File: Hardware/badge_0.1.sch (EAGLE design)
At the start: 59 parts, among them CON1 PH_2, IC1 CP2102, SW2 MK12C02, U1 SMBT2222A, U2 SMBT2222A, U4 MCP73832T-2DCI/OT

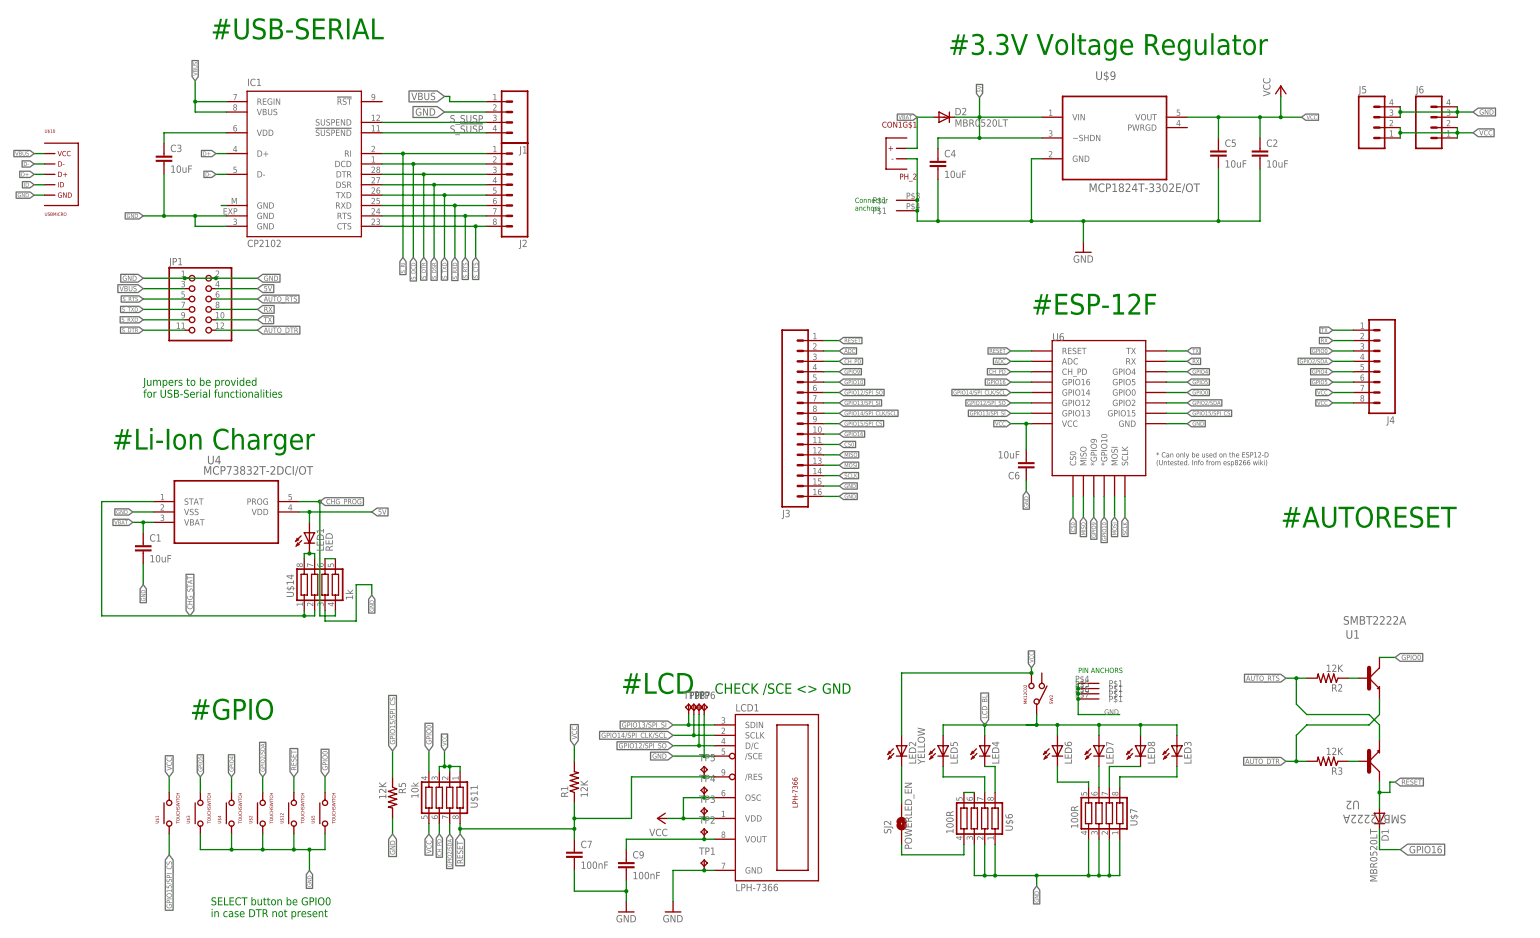
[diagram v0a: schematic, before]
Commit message: Replaced serial jumpers with a header. Thus removing the need to populate the jumpers during board assembly.
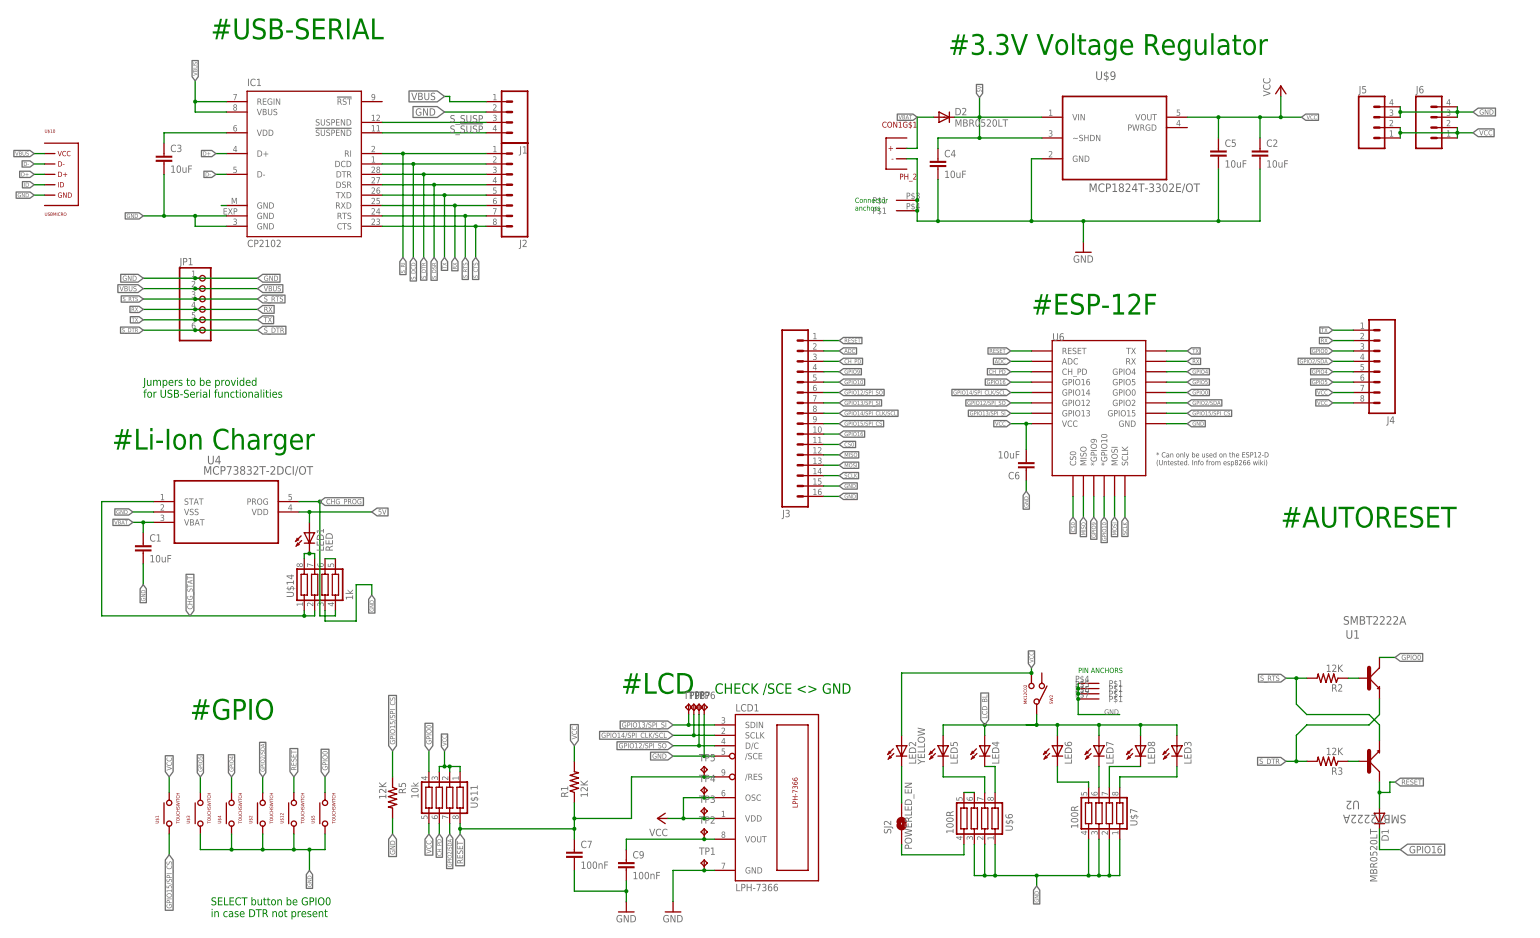
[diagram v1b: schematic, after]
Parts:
- JP1: device pinhead:PINHD-2X6 -> pinhead:PINHD-1X6
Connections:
- removed net AUTO_DTR: JP1.12, R3.2, U1.E
- removed net AUTO_RTS: JP1.6, R2.2, U2.E
- removed net S_RXD: IC1.RXD, J2.6, JP1.9
- removed net S_TXD: IC1.TXD, J2.5, JP1.7
- net 5V: no longer JP1.4
- net GND: no longer JP1.2
- net RX: now also IC1.RXD, J2.6, JP1.4; no longer JP1.8
- net S_DTR: now also JP1.6, R3.2, U1.E; no longer JP1.11
- net S_RTS: now also JP1.3, R2.2, U2.E; no longer JP1.5
- net TX: now also IC1.TXD, J2.5, JP1.5; no longer JP1.10
- net VBUS: now also JP1.2; no longer JP1.3

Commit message: Removed 12K resistor after connecting LCD & ESP resets.
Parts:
- removed R1: 12K, SparkFun-Passives:RESISTOR0805-RES
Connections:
- net RESET: no longer R1.1
- net VCC: no longer R1.2
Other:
- note added: "10K array"
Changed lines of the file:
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@@
 <part name="C6" library="SparkFun-Capacitors" deviceset="1UF-25V-10%(0805)" device="&quot;" value="10uF"/>
 <part name="C7" library="SparkFun-Capacitors" deviceset="1UF-25V-10%(0805)" device="&quot;" value="100nF"/>
-<part name="R1" library="SparkFun-Passives" deviceset="RESISTOR" device="0805-RES" value="12K"/>
 <part name="U1" library="badge" deviceset="SMBT2222A" device=""/>
 <part name="U2" library="badge" deviceset="SMBT2222A" device=""/>
@@
 anchors</text>
 <text x="271.78" y="88.9" size="1.27" layer="91" font="vector">PIN ANCHORS</text>
+<text x="148.59" y="62.23" size="1.778" layer="91" align="center">10K
+array</text>
 </plain>
 <instances>
@@
 <instance part="C6" gate="G$1" x="259.08" y="140.97" rot="R180"/>
 <instance part="C7" gate="G$1" x="148.59" y="43.18"/>
-<instance part="R1" gate="G$1" x="148.59" y="62.23" rot="R90"/>
 <instance part="U1" gate="A" x="342.9" y="87.63"/>
 <instance part="U2" gate="A" x="342.9" y="67.31" rot="MR180"/>
@@
 </segment>
 <segment>
-<pinref part="R1" gate="G$1" pin="2"/>
 <wire x1="148.59" y1="71.12" x2="148.59" y2="67.31" width="0.1524" layer="91"/>
 <label x="148.59" y="71.12" size="1.27" layer="95" rot="R90" xref="yes"/>
@@
 <pinref part="U$11" gate="G$1" pin="8"/>
 <wire x1="120.65" y1="52.07" x2="120.65" y2="50.8" width="0.1524" layer="91"/>
-<pinref part="R1" gate="G$1" pin="1"/>
 <pinref part="C7" gate="G$1" pin="1"/>
 <wire x1="120.65" y1="50.8" x2="120.65" y2="49.53" width="0.1524" layer="91"/>

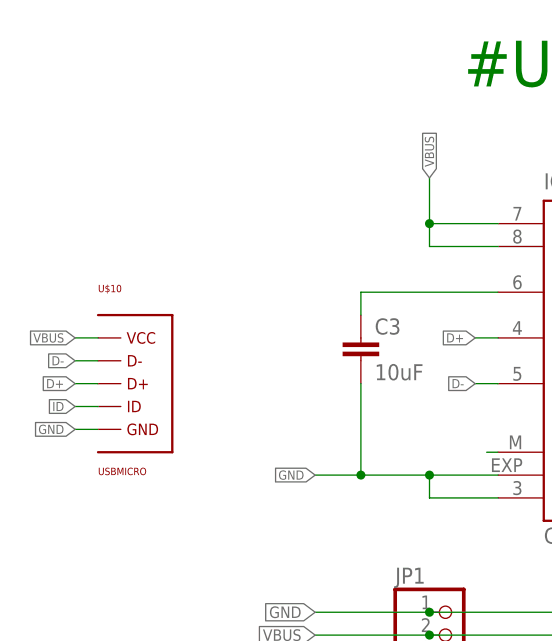
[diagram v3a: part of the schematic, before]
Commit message: moved pads and vias out of the way
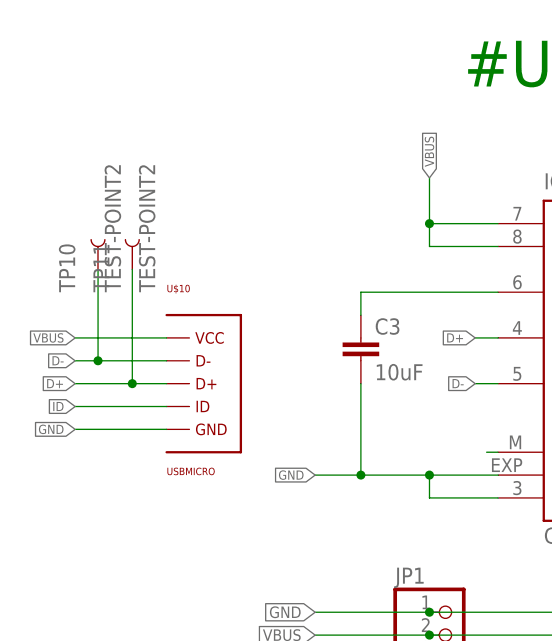
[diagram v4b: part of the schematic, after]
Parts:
- added TP10, TP11: TEST-POINT2, SparkFun-Passives:TEST-POINT2
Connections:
- net D+: now also TP11.1
- net D-: now also TP10.1
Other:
- moved on the sheet: U$10
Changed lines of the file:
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@@
 <setting verticaltext="up"/>
 </settings>
-<grid distance="0.1" unitdist="inch" unit="inch" style="lines" multiple="1" display="no" altdistance="0.01" altunitdist="inch" altunit="inch"/>
+<grid distance="0.05" unitdist="inch" unit="inch" style="lines" multiple="1" display="no" altdistance="0.01" altunitdist="inch" altunit="inch"/>
 <layers>
 <layer number="1" name="Top" color="4" fill="1" visible="no" active="no"/>
@@
 <part name="C2" library="SparkFun-Capacitors" deviceset="1UF-25V-10%(0805)" device="&quot;" value="10uF"/>
 <part name="JP1" library="pinhead" deviceset="PINHD-1X6" device=""/>
+<part name="TP10" library="SparkFun-Passives" deviceset="TEST-POINT" device="2" value="TEST-POINT2"/>
+<part name="TP11" library="SparkFun-Passives" deviceset="TEST-POINT" device="2" value="TEST-POINT2"/>
 </parts>
 <sheets>
@@
 <instance part="U6" gate="G$1" x="278.13" y="160.02"/>
 <instance part="U$9" gate="A" x="280.67" y="222.25"/>
-<instance part="U$10" gate="G$1" x="24.13" y="210.82"/>
+<instance part="U$10" gate="G$1" x="31.75" y="210.82"/>
 <instance part="LED1" gate="G$1" x="83.82" y="123.19"/>
 <instance part="LED2" gate="G$1" x="228.6" y="71.12"/>
@@
 <instance part="SW2" gate="G$4" x="276.86" y="83.82"/>
 <instance part="JP1" gate="A" x="58.42" y="177.8"/>
+<instance part="TP10" gate="G$1" x="19.05" y="223.52" rot="R90"/>
+<instance part="TP11" gate="G$1" x="22.86" y="223.52" rot="R90"/>
 </instances>
 <busses>
@@
 <segment>
 <pinref part="U$10" gate="G$1" pin="P$GND"/>
-<wire x1="16.51" y1="205.74" x2="19.05" y2="205.74" width="0.1524" layer="91"/>
+<wire x1="16.51" y1="205.74" x2="26.67" y2="205.74" width="0.1524" layer="91"/>
 <label x="16.51" y="205.74" size="1.016" layer="95" rot="R180" xref="yes"/>
 </segment>
@@
 <segment>
 <pinref part="U$10" gate="G$1" pin="P$VCC"/>
-<wire x1="16.51" y1="215.9" x2="19.05" y2="215.9" width="0.1524" layer="91"/>
+<wire x1="16.51" y1="215.9" x2="26.67" y2="215.9" width="0.1524" layer="91"/>
 <label x="16.51" y="215.9" size="1.016" layer="95" rot="R180" xref="yes"/>
 </segment>
@@
 <wire x1="16.51" y1="213.36" x2="19.05" y2="213.36" width="0.1524" layer="91"/>
 <label x="16.51" y="213.36" size="1.016" layer="95" rot="R180" xref="yes"/>
+<pinref part="TP10" gate="G$1" pin="1"/>
+<wire x1="19.05" y1="213.36" x2="26.67" y2="213.36" width="0.1524" layer="91"/>
+<wire x1="19.05" y1="223.52" x2="19.05" y2="213.36" width="0.1524" layer="91"/>
+<junction x="19.05" y="213.36"/>
 </segment>
 <segment>
@@
 <segment>
 <pinref part="U$10" gate="G$1" pin="P$D+"/>
-<wire x1="16.51" y1="210.82" x2="19.05" y2="210.82" width="0.1524" layer="91"/>
+<wire x1="16.51" y1="210.82" x2="22.86" y2="210.82" width="0.1524" layer="91"/>
 <label x="16.51" y="210.82" size="1.016" layer="95" rot="R180" xref="yes"/>
+<pinref part="TP11" gate="G$1" pin="1"/>
+<wire x1="22.86" y1="210.82" x2="26.67" y2="210.82" width="0.1524" layer="91"/>
+<wire x1="22.86" y1="223.52" x2="22.86" y2="210.82" width="0.1524" layer="91"/>
+<junction x="22.86" y="210.82"/>
 </segment>
 <segment>
@@
 <segment>
 <pinref part="U$10" gate="G$1" pin="P$ID"/>
-<wire x1="16.51" y1="208.28" x2="19.05" y2="208.28" width="0.1524" layer="91"/>
+<wire x1="16.51" y1="208.28" x2="26.67" y2="208.28" width="0.1524" layer="91"/>
 <label x="16.51" y="208.28" size="1.016" layer="95" rot="R180" xref="yes"/>
 </segment>

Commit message: okey dokey
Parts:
- removed R2, R3: 12K, SparkFun-Passives:RESISTOR0805-RES
- removed U1, U2: SMBT2222A, badge:SMBT2222A
- added IC2: PIMH9, badge:PIMH9
- added J7: 2X6 FEMALE, SparkFun-Connectors:M06X2PTH_FEMALE
- added JP2, JP3, JP4, JP6: JUMPER-PAD-2-NOJELLY, SparkFun-Passives:JUMPER-PAD-2-NOJELLY
- J1: device SparkFun-Connectors:M04PTH -> SparkFun-Connectors:M03PTH
- JP1: value (none) -> JUMPER-PAD-2-NOJELLY; device pinhead:PINHD-1X6 -> SparkFun-Passives:JUMPER-PAD-2-NOJELLY
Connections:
- removed net N$10: R2.1, U1.B
- removed net N$3: R3.1, U2.B
- removed net S_!SUSP: IC1.!SUSPEND, J1.4
- new net DTR: IC2.P$2, IC2.P$4, J7.12, JP1.1
- new net RTS: IC2.P$1, IC2.P$5, J7.6, JP6.1
- new net S_RX: IC1.RXD, J2.6, J7.9, JP2.2
- new net S_TX: IC1.TXD, J2.5, J7.7, JP3.2
- net 5V: now also J7.4, JP4.2
- net GND: now also J7.1, J7.2; no longer JP1.1
- net GPIO0: now also IC2.P$3; no longer U1.C
- net RESET: now also IC2.P$6; no longer U2.C
- net RX: now also J7.8, JP3.1; no longer IC1.RXD, J2.6, JP1.4
- net S_DTR: now also J7.11, JP1.2; no longer JP1.6, R3.2, U1.E
- net S_RTS: now also J7.5, JP6.2; no longer JP1.3, R2.2, U2.E
- net TX: now also J7.10, JP2.1; no longer IC1.TXD, J2.5, JP1.5
- net VBUS: now also J7.3, JP4.1; no longer JP1.2
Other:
- note removed: "10K array"
- moved on the sheet: D1

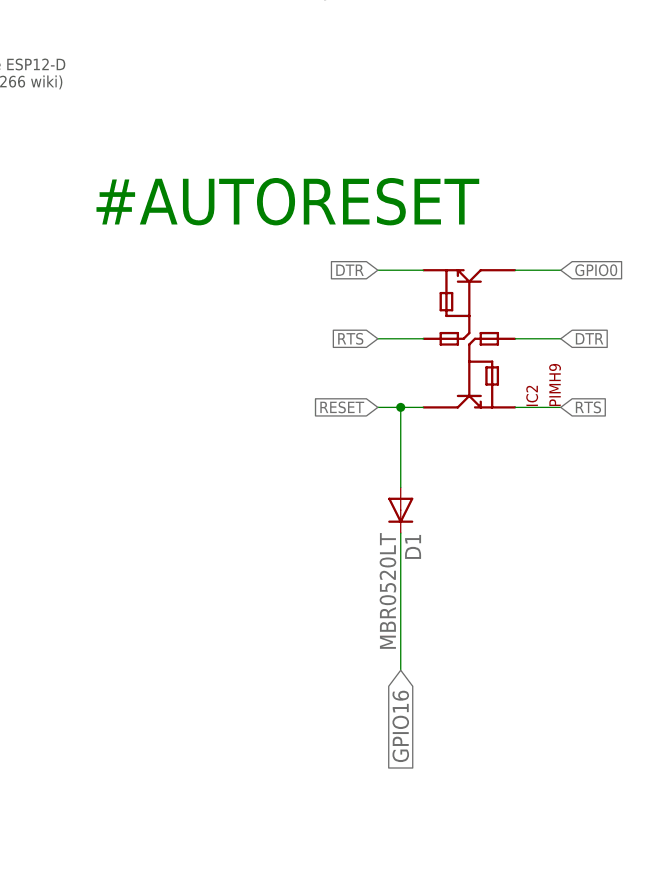
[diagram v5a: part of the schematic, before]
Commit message: Added deep-sleep jumper point (closed by default); More routing optimizations
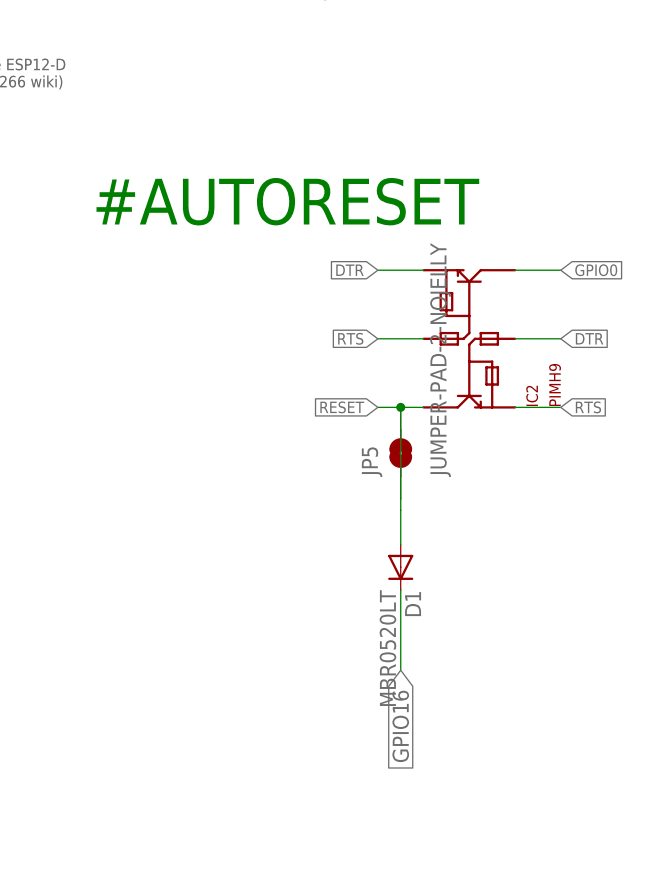
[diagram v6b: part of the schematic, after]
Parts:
- added JP5: JUMPER-PAD-2-NOJELLY, SparkFun-Passives:JUMPER-PAD-2-NOJELLY
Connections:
- net RESET: now also JP5.1, JP5.2
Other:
- moved on the sheet: D1
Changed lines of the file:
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@@
 <?xml version="1.0" encoding="utf-8"?>
 <!DOCTYPE eagle SYSTEM "eagle.dtd">
-<eagle version="7.5.0">
+<eagle version="7.1.0">
 <drawing>
 <settings>
@@
 <part name="JP3" library="SparkFun-Passives" deviceset="JUMPER-PAD-2-NO" device="JELLY" value="JUMPER-PAD-2-NOJELLY"/>
 <part name="JP4" library="SparkFun-Passives" deviceset="JUMPER-PAD-2-NO" device="JELLY" value="JUMPER-PAD-2-NOJELLY"/>
+<part name="JP5" library="SparkFun-Passives" deviceset="JUMPER-PAD-2-NO" device="JELLY" value="JUMPER-PAD-2-NOJELLY"/>
 </parts>
 <sheets>
@@
 <instance part="TP8" gate="G$1" x="177.8" y="81.28"/>
 <instance part="TP9" gate="G$1" x="176.53" y="81.28"/>
-<instance part="D1" gate="G$1" x="355.6" y="92.71" rot="R270"/>
+<instance part="D1" gate="G$1" x="355.6" y="86.36" rot="R270"/>
 <instance part="D2" gate="G$1" x="239.014" y="224.79"/>
 <instance part="C2" gate="G$1" x="316.23" y="214.63"/>
@@
 <instance part="JP3" gate="G$1" x="166.37" y="148.59" rot="R90"/>
 <instance part="JP4" gate="G$1" x="124.46" y="148.59" rot="R90"/>
+<instance part="JP5" gate="G$1" x="355.6" y="99.06" rot="R90"/>
 </instances>
 <busses>
@@
 <segment>
 <pinref part="IC2" gate="G$1" pin="P$6"/>
+<label x="353.06" y="104.14" size="1.27" layer="95" rot="R180" xref="yes"/>
 <wire x1="358.14" y1="104.14" x2="355.6" y2="104.14" width="0.1524" layer="91"/>
-<label x="353.06" y="104.14" size="1.27" layer="95" rot="R180" xref="yes"/>
+<pinref part="JP5" gate="G$1" pin="2"/>
 <wire x1="355.6" y1="104.14" x2="353.06" y2="104.14" width="0.1524" layer="91"/>
+<junction x="355.6" y="104.14"/>
+<pinref part="JP5" gate="G$1" pin="1"/>
 <pinref part="D1" gate="G$1" pin="A"/>
-<wire x1="355.6" y1="104.14" x2="355.6" y2="95.25" width="0.1524" layer="91"/>
-<junction x="355.6" y="104.14"/>
+<wire x1="355.6" y1="93.98" x2="355.6" y2="92.71" width="0.1524" layer="91"/>
+<wire x1="355.6" y1="92.71" x2="355.6" y2="88.9" width="0.1524" layer="91"/>
+<wire x1="355.6" y1="104.14" x2="355.6" y2="93.98" width="0.1524" layer="91"/>
 </segment>
 </net>
@@
 <segment>
 <pinref part="D1" gate="G$1" pin="C"/>
-<wire x1="355.6" y1="90.17" x2="355.6" y2="74.93" width="0.1524" layer="91"/>
+<wire x1="355.6" y1="83.82" x2="355.6" y2="74.93" width="0.1524" layer="91"/>
 <label x="355.6" y="74.93" size="1.778" layer="95" rot="R270" xref="yes"/>
 </segment>
